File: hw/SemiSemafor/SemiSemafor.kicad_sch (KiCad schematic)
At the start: 24 parts, among them J1 USB_PCB, SW1 SW_DIP_x01, U1 LD39200, U2 ESP32-C3-MINI-1

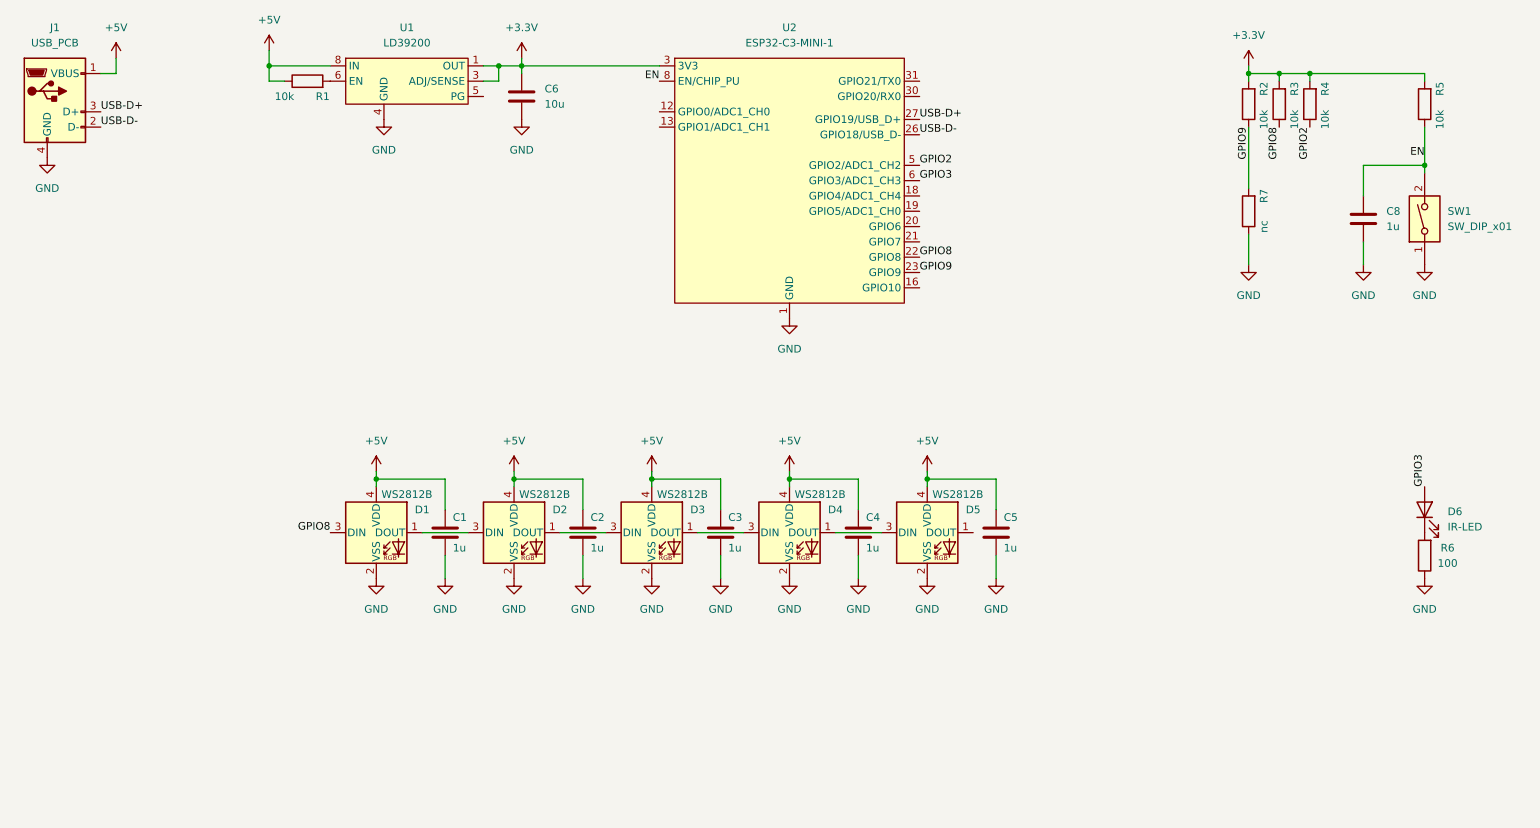
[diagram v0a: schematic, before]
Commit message: Change button connection
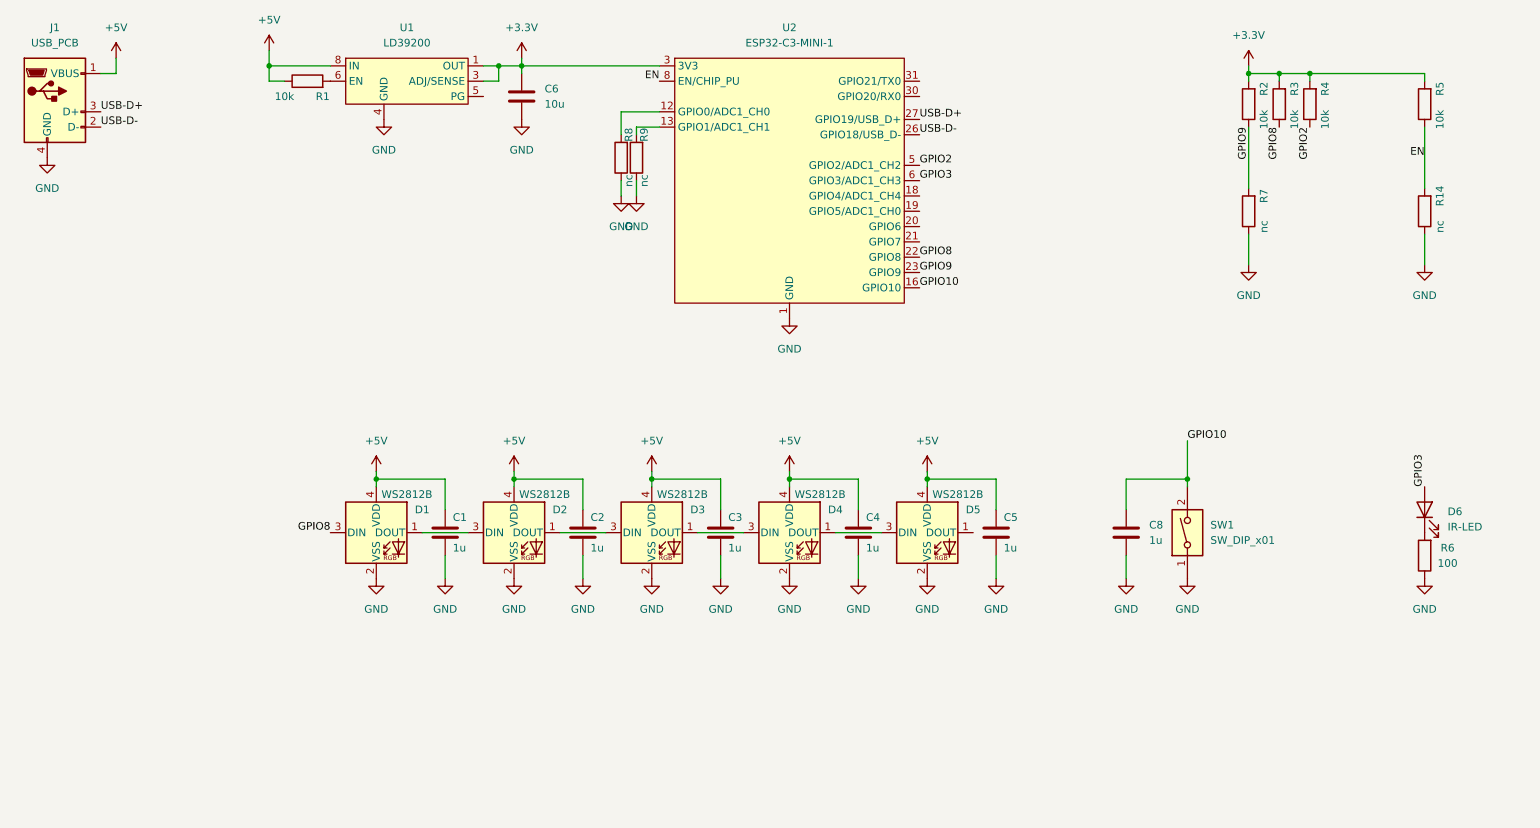
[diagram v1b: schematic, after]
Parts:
- added R14, R8, R9: nc, Resistor_SMD:R_0402_1005Metric, symbol Device:R
- U1: JLCPCB_CORRECTION 0;0;90 -> 0;0;270
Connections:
- net EN: now also R14.2; no longer C8.1, SW1.2
- net GND: now also R14.1, R8.1, R9.1
- net at U2.12 (GPIO0/ADC1_CH0): now also R8.2
- net at U2.13 (GPIO1/ADC1_CH1): now also R9.2
- net GPIO10: now reaches U2.16 (GPIO10)
- net GPIO10: now also C8.1, SW1.2
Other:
- moved on the sheet: C8, SW1

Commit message: fix LDO
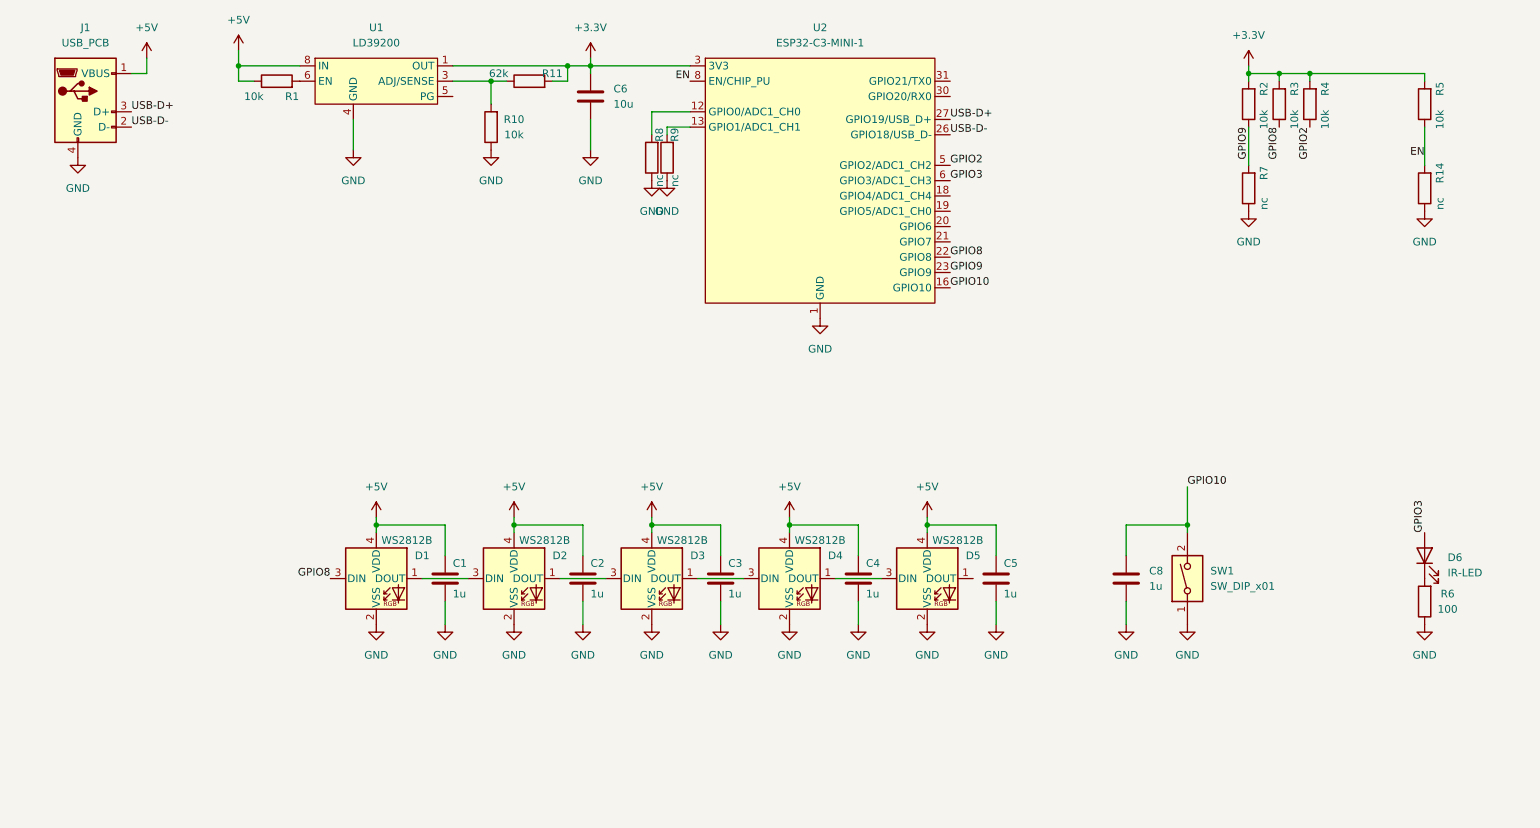
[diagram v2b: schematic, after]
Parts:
- added R10: 10k, Resistor_SMD:R_0402_1005Metric, symbol Device:R
- added R11: 62k, Resistor_SMD:R_0402_1005Metric, symbol Device:R
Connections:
- net +3.3V: now also R11.2; no longer U1.3 (ADJ/SENSE)
- net GND: now also R10.1
- new net: R10.2, R11.1, U1.3 (ADJ/SENSE)
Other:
- moved on the sheet: C1, C2, C3, C4, C5, C6, C8, D1, D2, D3, D4, D5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

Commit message: Fix LDO, add button and programming connector
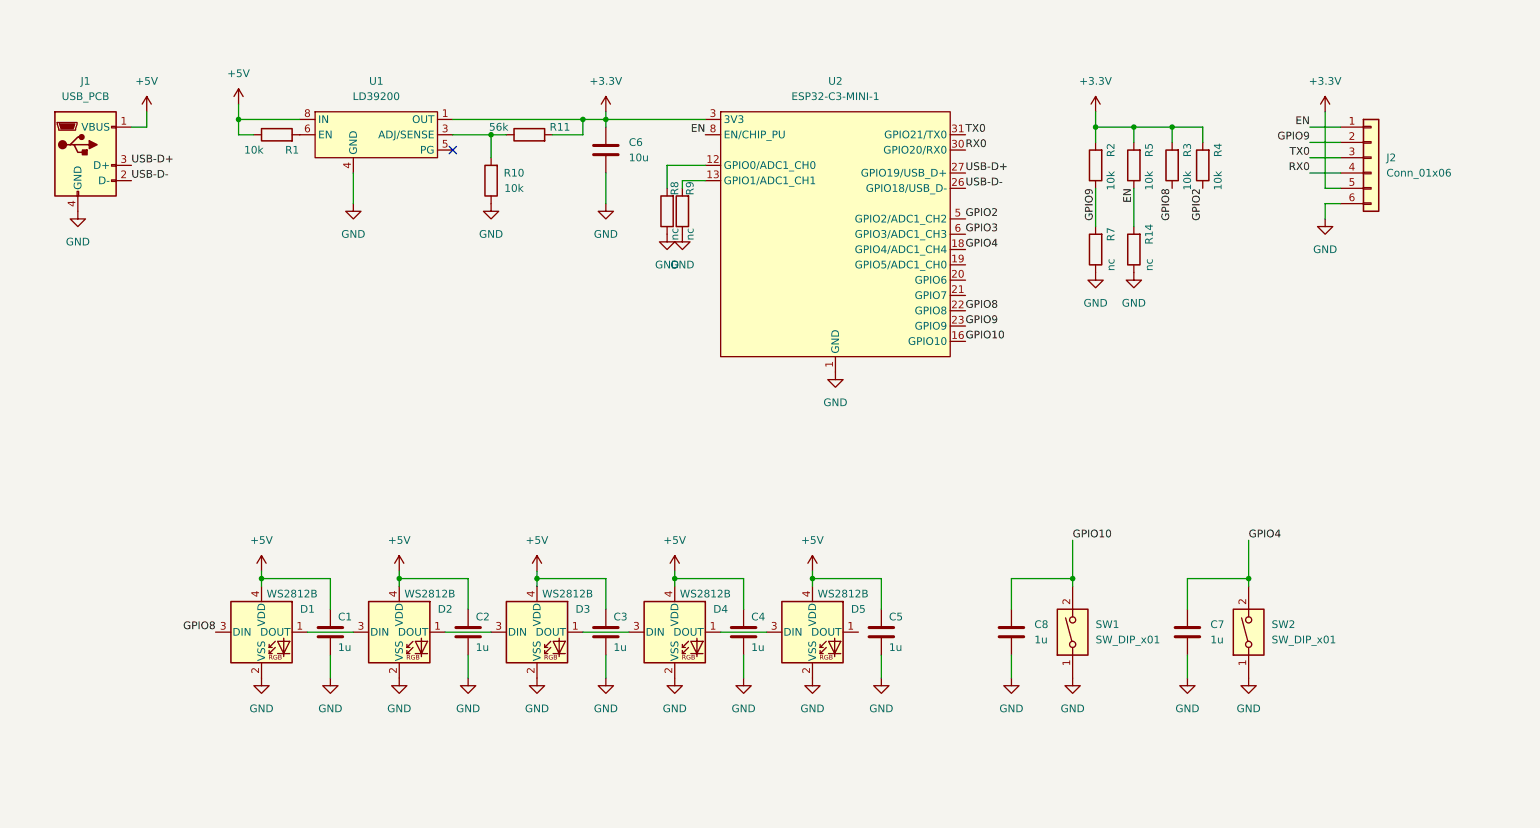
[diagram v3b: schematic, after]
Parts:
- removed D6: IR-LED, LED_SMD:LED_0603_1608Metric, symbol Device:LED
- removed R6: 100, Resistor_SMD:R_0402_1005Metric, symbol Device:R
- added C7: 1u, Capacitor_SMD:C_0402_1005Metric, symbol Device:C
- added J2: Conn_01x06, Connector_PinHeader_1.00mm:PinHeader_1x06_P1.00mm_Vertical, symbol Connector_Generic:Conn_01x06
- added SW2: SW_DIP_x01, Button_Switch_SMD:SW_Push_1P1T_NO_Vertical_Wuerth_434133025816, symbol Switch:SW_DIP_x01
- R11: value 62k -> 56k; LCSC C37825 -> C25796
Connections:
- net +3.3V: now also J2.5 (Pin_5)
- net EN: now also J2.1 (Pin_1)
- net GND: now also C7.2, J2.6 (Pin_6), SW2.1
- net GPIO9: now also J2.2 (Pin_2)
- net GPIO4: now reaches U2.18 (GPIO4/ADC1_CH4)
- net GPIO4: now also C7.1, SW2.2
- net RX0: now reaches U2.30 (GPIO20/RX0)
- net RX0: now also J2.4 (Pin_4)
- net TX0: now reaches U2.31 (GPIO21/TX0)
- net TX0: now also J2.3 (Pin_3)
- no-connect marks 0 -> 1
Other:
- moved on the sheet: C1, C2, C3, C4, C5, C6, C8, D1, D2, D3, D4, D5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

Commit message: PCB
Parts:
- removed J2: Conn_01x06, Connector_PinHeader_1.00mm:PinHeader_1x06_P1.00mm_Vertical, symbol Connector_Generic:Conn_01x06
- removed R1: 10k, Resistor_SMD:R_0402_1005Metric, symbol Device:R
- removed R14, R7, R8, R9: nc, Resistor_SMD:R_0402_1005Metric, symbol Device:R
- added FB1: FerriteBead, Inductor_SMD:L_0201_0603Metric, symbol Device:FerriteBead
- added J2: ESP-Programing_conector, Robotarna_KiCad_Library:ESP-Programing_conector, symbol Robotarna_KiCad_Library:ESP-Programing_conector
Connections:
- net +5V: now also U1.6 (EN), J2.1 (VCC)
- net EN: now also J2.3 (EN)
- net GND: now also U2.11 (GND), U2.14 (GND), U2.2 (GND), U2.36 (GND), U2.37 (GND), U2.38 (GND), U2.39 (GND), U2.40 (GND), U2.41 (GND), U2.42 (GND), U2.43 (GND), U2.44 (GND), U2.45 (GND), U2.46 (GND), U2.47 (GND), U2.48 (GND), U2.49 (GND), J2.2 (GND)
- net RX0: now also J2.5 (RX)
- net TX0: now also J2.6 (TX)
- net SW1: now reaches U2.13 (GPIO1/ADC1_CH1)
- net SW1: now also C7.1, SW2.2
- net SW0: now reaches U2.12 (GPIO0/ADC1_CH0)
- net SW0: now also C8.1, SW1.2
- removed net GPIO10: C8.1, SW1.2, U2.16 (GPIO10)
- net GPIO3: no longer names the net of U2.6 (GPIO3/ADC1_CH3)
- removed net GPIO4: C7.1, SW2.2, U2.18 (GPIO4/ADC1_CH4)
- net GPIO8 renamed I-LED
- net I-LED: now also FB1.1; no longer D1.3 (DIN)
- net GPIO9 renamed BOOT
- net BOOT: now also J2.4 (BOOT)
- new net: D1.3 (DIN), FB1.2
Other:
- moved on the sheet: C6, J1, R10, R11, R2, R3, R4, R5, U1, U2

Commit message: Polygon and rout tracks correction
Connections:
- net GND: now also U2.50 (GND), U2.51 (GND), U2.52 (GND), U2.53 (GND)
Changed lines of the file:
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@@
     (pin "49")
     (pin "5")
+    (pin "50")
+    (pin "51")
+    (pin "52")
+    (pin "53")
     (pin "6")
     (pin "8")

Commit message: 12 LED
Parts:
- added C10, C11, C12, C13, C14, C15, C9: 1u, Capacitor_SMD:C_0402_1005Metric, symbol Device:C
- added D10, D11, D12, D6, D7, D8, D9: WS2812B, LED_SMD:LED_WS2812B-2020_PLCC4_2.0x2.0mm, symbol LED:WS2812B
- U2: JLCPCB_CORRECTION 0;0;180 -> (none); LCSC C2935306 -> C2838502
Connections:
- net +5V: now also C10.1, C11.1, C12.1, C13.1, C14.1, C15.1, C9.1, D10.4 (VDD), D11.4 (VDD), D12.4 (VDD), D6.4 (VDD), D7.4 (VDD), D8.4 (VDD), D9.4 (VDD)
- net GND: now also C10.2, C11.2, C12.2, C13.2, C14.2, C15.2, C9.2, D10.2 (VSS), D11.2 (VSS), D12.2 (VSS), D6.2 (VSS), D7.2 (VSS), D8.2 (VSS), D9.2 (VSS)
- net at D5.1 (DOUT): now also D11.3 (DIN)
- net SW0 renamed SW2
- new net: D8.1 (DOUT), D9.3 (DIN)
- new net: D7.1 (DOUT), D8.3 (DIN)
- new net: D10.3 (DIN), D9.1 (DOUT)
- new net: D10.1 (DOUT), D12.3 (DIN)
- new net: D6.1 (DOUT), D7.3 (DIN)
- new net: D11.1 (DOUT), D6.3 (DIN)
- no-connect marks 1 -> 2
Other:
- moved on the sheet: C1, C2, C3, C4, C5, C7, C8, D1, D2, D3, D4, D5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
